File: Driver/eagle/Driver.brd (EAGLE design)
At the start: 100 x 80 mm, 32 parts, among them U1 L6205PDES, X1 22-23-2021, X2 22-23-2021, X3 22-23-2021

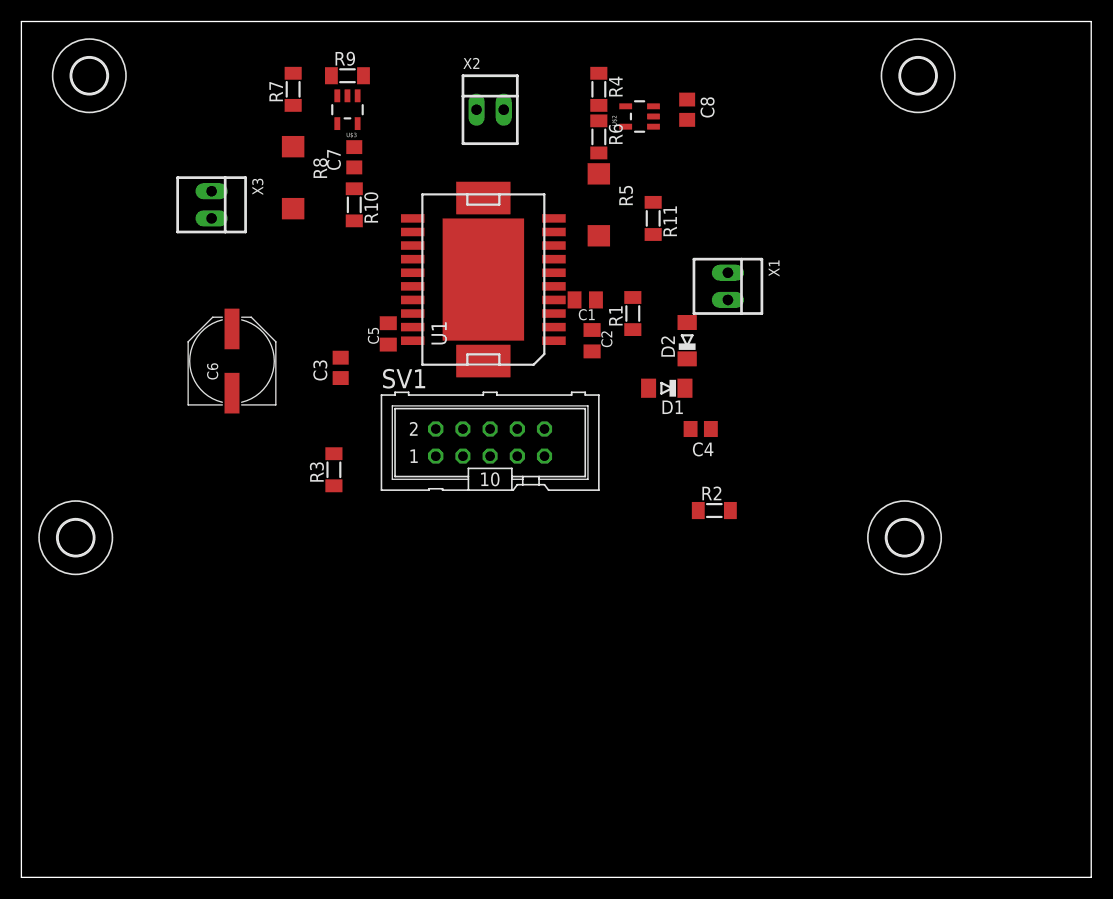
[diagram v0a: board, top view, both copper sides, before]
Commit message: update driver layout
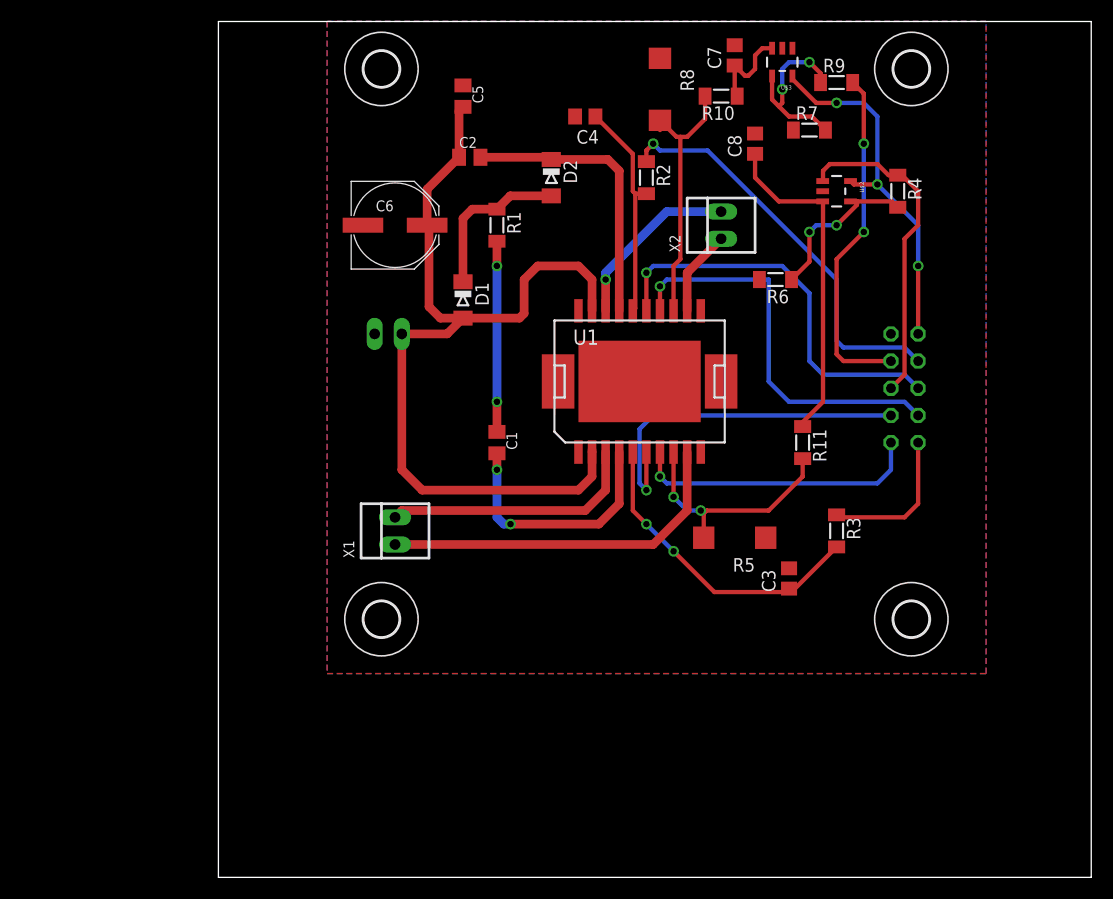
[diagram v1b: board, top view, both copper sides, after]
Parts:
- moved R7 48.4 mm to (73.7, 69.8), turned to 0 degrees
- moved R3 47.3 mm to (76.2, 32.4), turned to 270 degrees
- moved C3 46.3 mm to (71.8, 27.9)
- moved R9 45.7 mm to (76.2, 74.3)
- moved U$3 40.9 mm to (72.4, 78.7)
- moved SV1 39.1 mm to (82.5, 45.7), flipped to the bottom, turned to 90 degrees
- moved X1 38.6 mm to (34.9, 32.4), turned to 90 degrees
- moved C7 36.8 mm to (66.7, 76.8)
- moved R10 35.8 mm to (65.4, 73.0), turned to 180 degrees
- moved R8 35.3 mm to (59.7, 73.7)
- moved R5 33.6 mm to (66.7, 31.8), turned to 180 degrees
- moved R2 31.8 mm to (58.4, 65.4), turned to 270 degrees
- moved C4 31.1 mm to (52.7, 71.1)
- moved H4 29.6 mm to (33.7, 24.1)
- moved R4 29.5 mm to (81.9, 64.1)
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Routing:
- net N$1: track 0.00 -> 83.8 mm
- net N$11: track 0.00 -> 38.5 mm, vias 0 -> 1
- net N$8: track 0.00 -> 37.7 mm, vias 0 -> 1
- net N$10: track 0.00 -> 37.5 mm, vias 0 -> 1
- net +5V: track 0.00 -> 34.2 mm, vias 0 -> 3
- net N$23: track 0.00 -> 34.1 mm
- net N$6: track 0.00 -> 33.6 mm, vias 0 -> 1
- net N$25: track 0.00 -> 32.2 mm, vias 0 -> 2
- net N$16: track 0.00 -> 31.3 mm
- net N$17: track 0.00 -> 30.6 mm
- net N$9: track 0.00 -> 29.4 mm, vias 0 -> 2
- net N$12: track 0.00 -> 27.2 mm, vias 0 -> 1
- net N$5: track 0.00 -> 26.6 mm
- net N$13: track 0.00 -> 25.1 mm
- net N$22: track 0.00 -> 24.3 mm
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- added copper zone on layer 1, net GND
- added copper zone on layer 16, net GND
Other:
- board size 100 x 80 mm -> 81.6 x 80 mm

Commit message: Updated driver schematic
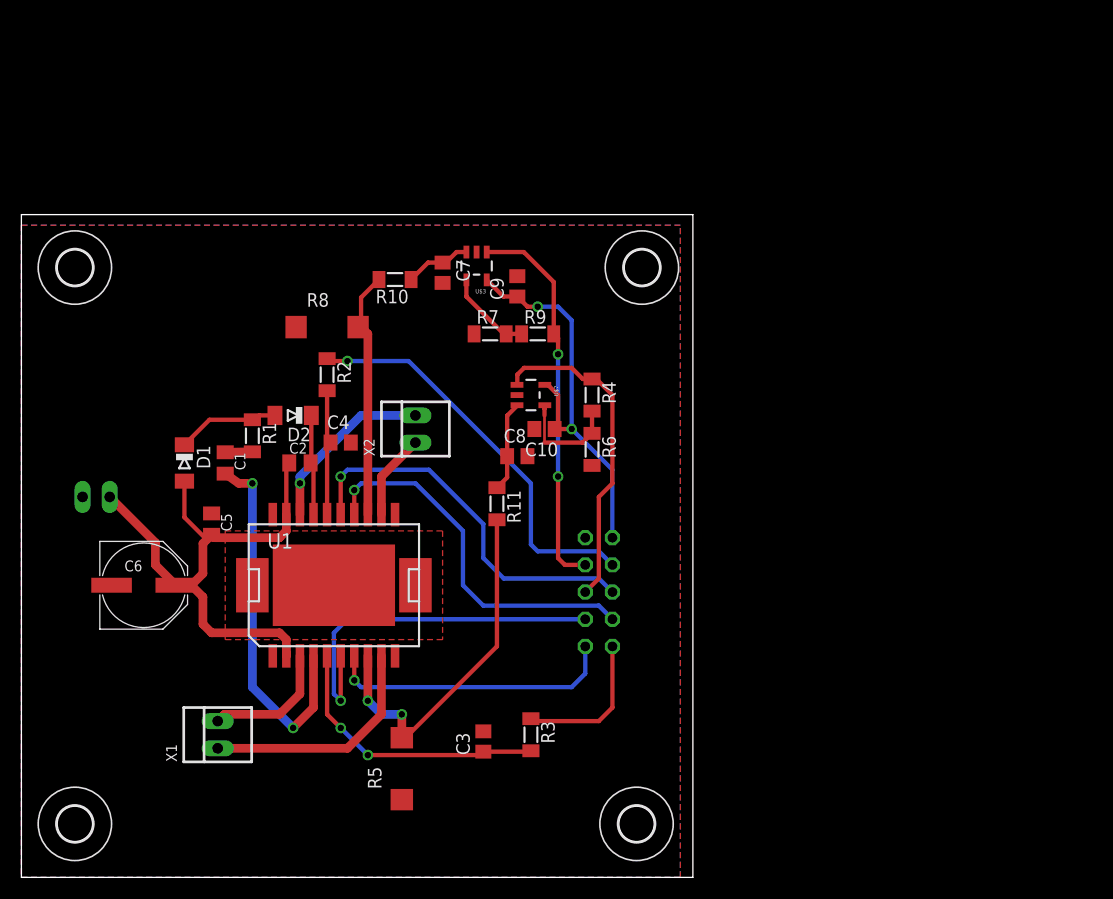
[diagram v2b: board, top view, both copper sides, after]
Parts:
- added C10, C9: (no value), rcl:C0805
- moved C5 46.4 mm to (17.8, 33.0)
- moved C6 41.0 mm to (11.4, 27.3)
- moved R8 38.2 mm to (28.6, 51.4), turned to 0 degrees
- moved C4 38.1 mm to (29.8, 40.6), turned to 0 degrees
- moved R5 37.9 mm to (35.6, 10.2), turned to 90 degrees
- moved C8 36.7 mm to (46.4, 39.4), turned to 0 degrees
- moved R9 36.5 mm to (48.3, 50.8)
- moved R7 35.4 mm to (43.8, 50.8)
- moved R2 35.1 mm to (28.6, 47.0)
- moved R10 35.0 mm to (34.9, 55.9)
- moved H4 34.5 mm to (5.00, 5.00)
- moved R4 34.3 mm to (53.3, 45.1)
- moved U$2 34.3 mm to (45.1, 46.4)
- moved X2 34.3 mm to (36.8, 41.9)
- moved R3 34.3 mm to (47.6, 13.3)
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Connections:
- net +5V: now also C10.1, C9.1
- net GND: now also C10.2, C9.2, U1.SLUG1, U1.SLUG2, U1.SLUG3
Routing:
- net N$1: track 83.8 -> 52.2 mm
- net N$16: track 31.3 -> 8.51 mm
- net N$5: track 26.6 -> 9.41 mm
- net N$3: track 17.8 -> 2.54 mm, vias 2 -> 0
- net N$19: track 22.3 -> 35.1 mm
- net N$23: track 34.1 -> 22.1 mm
- net N$22: track 24.3 -> 12.3 mm
- net N$4: track 23.3 -> 34.8 mm
- net N$26: track 17.1 -> 8.17 mm, vias 2 -> 0
- net N$15: track 20.8 -> 11.9 mm
- net N$2: track 15.0 -> 9.60 mm
- net N$18: track 15.6 -> 10.4 mm, vias 2 -> 0
- net +5V: track 34.2 -> 38.2 mm, vias 3 -> 2
- net N$25: track 32.2 -> 36.2 mm
- net N$9: track 29.4 -> 26.3 mm
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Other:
- board size 81.6 x 80 mm -> 62.8 x 62 mm
